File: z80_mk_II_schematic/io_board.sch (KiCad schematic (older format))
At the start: 27 parts, among them J2 Conn_02x10_Odd_Even, J3 Conn_02x08_Odd_Even, J4 Conn_02x10_Odd_Even, U12 74LS00, U13 Z80_PIO, U14 74LS245, U15 74LS145, U16 74LS245, U17 Z80_CTC, U18 74LS138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

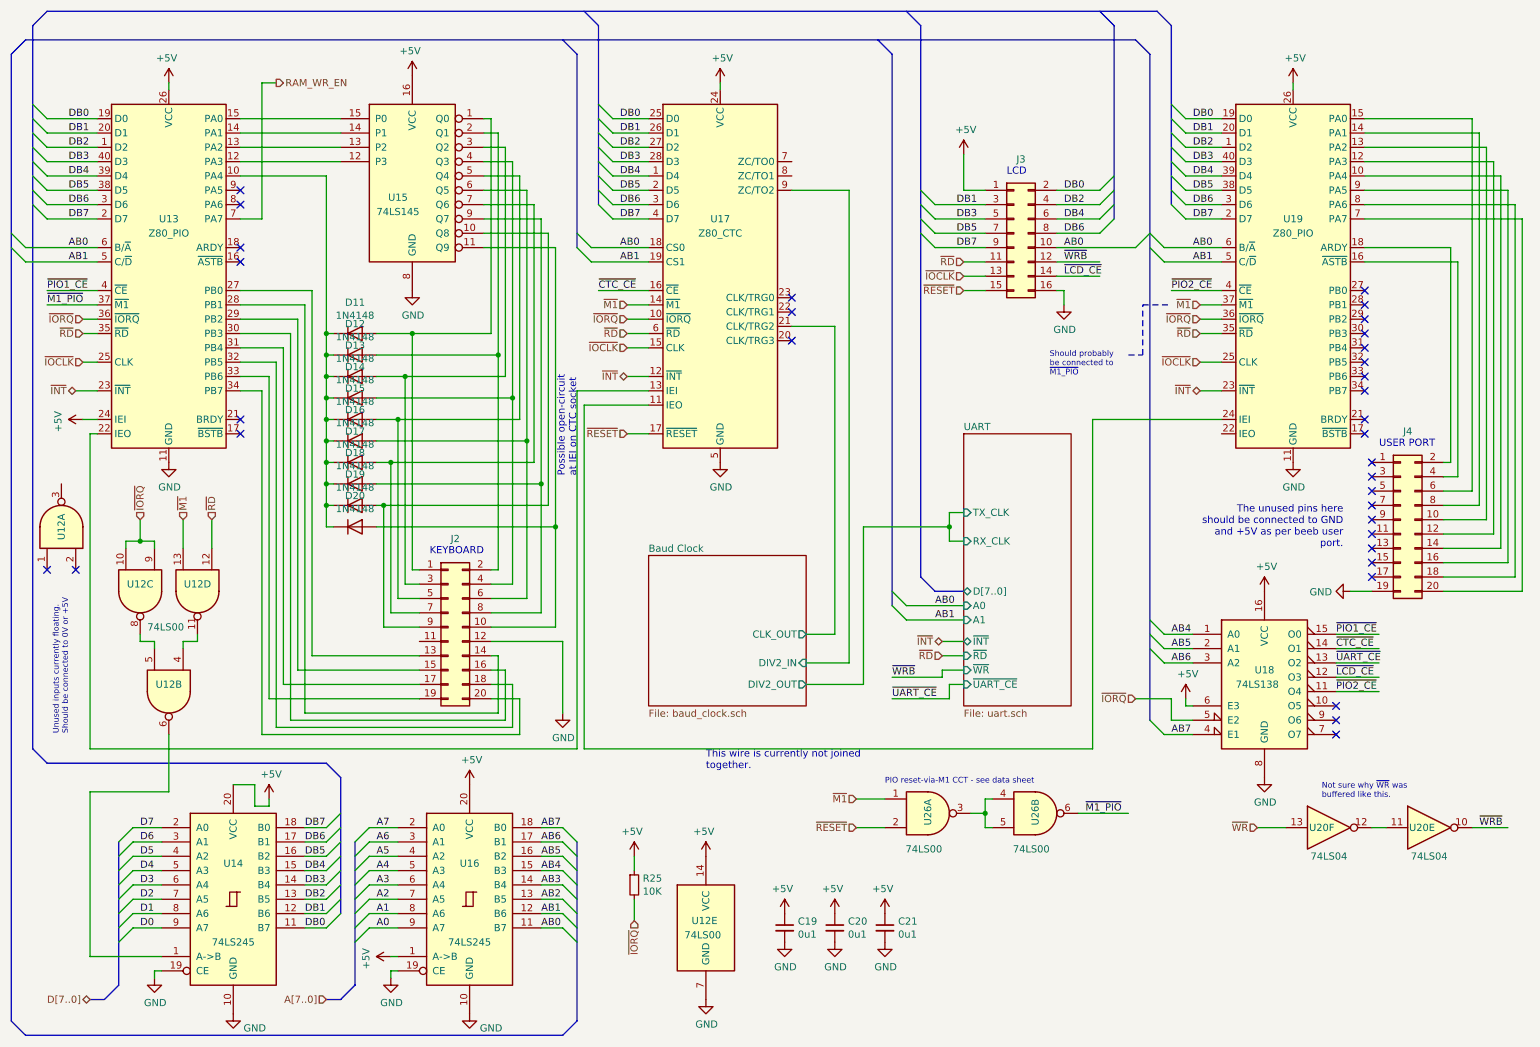
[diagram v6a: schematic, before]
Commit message: Add missing resnet for keyboard pull-ups.
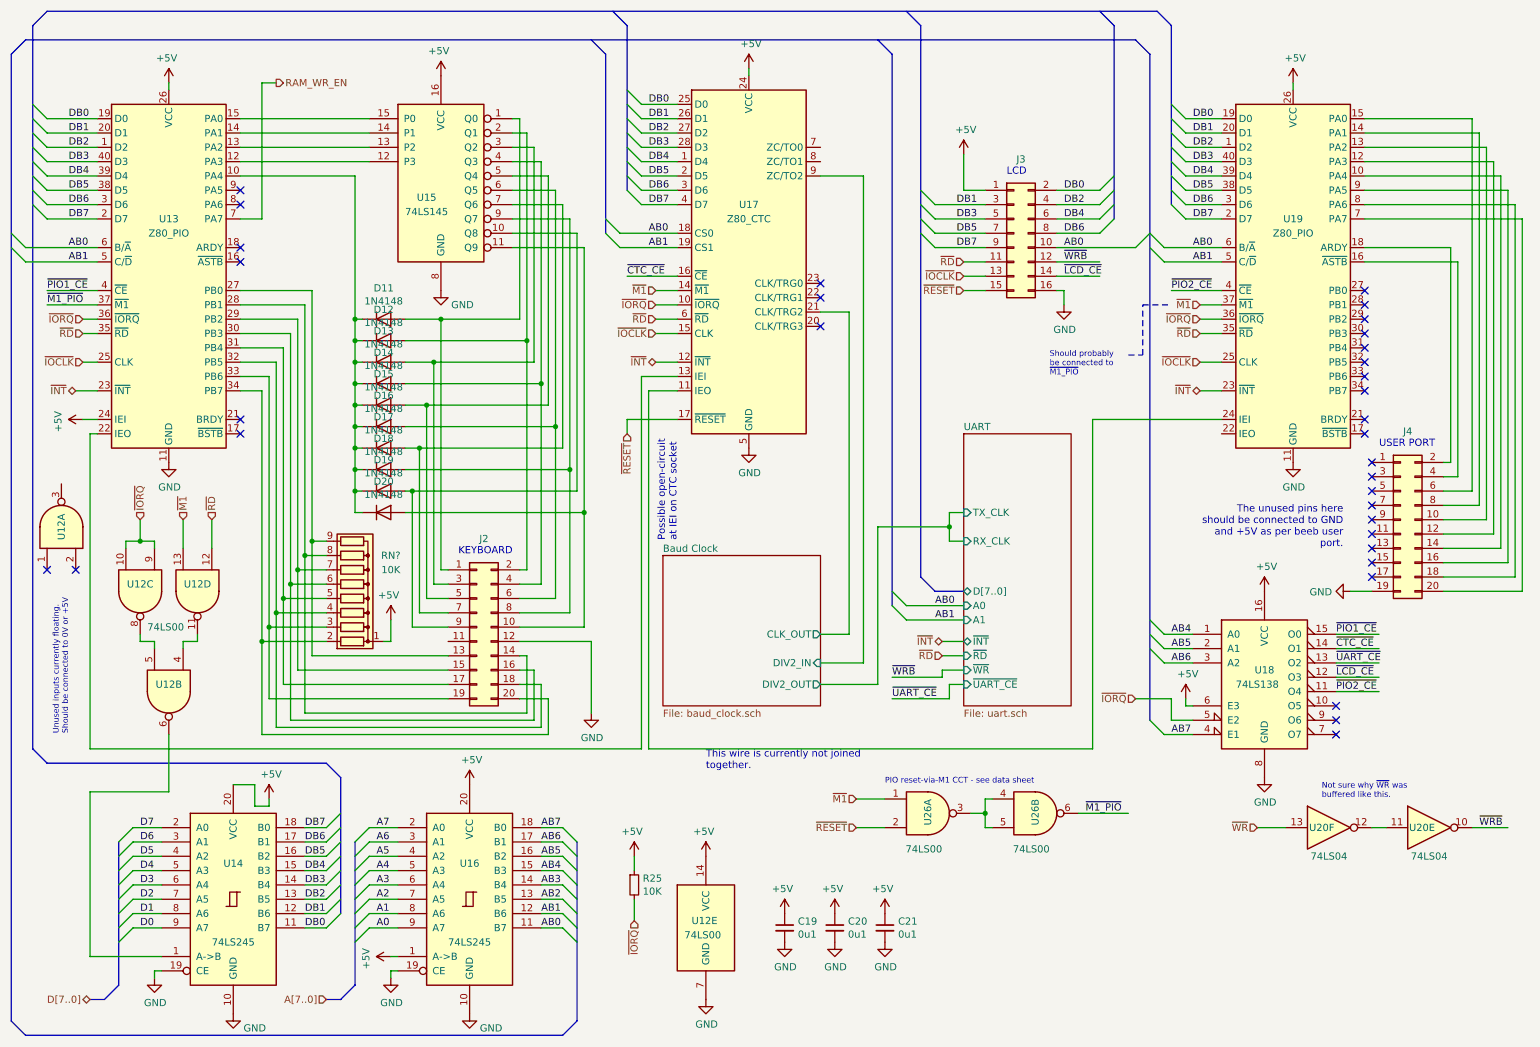
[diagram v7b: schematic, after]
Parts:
- added RN?: 10K, Resistor_THT:R_Array_SIP9, symbol Device:R_Network08
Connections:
- net +5V: now also RN?.1 (common)
- net at J2.13 (Pin_13), U13.27 (PB0): now also RN?.9 (R8)
- net at J2.14 (Pin_14), U13.28 (PB1): now also RN?.8 (R7)
- net at J2.15 (Pin_15), U13.29 (PB2): now also RN?.7 (R6)
- net at J2.16 (Pin_16), U13.30 (PB3): now also RN?.6 (R5)
- net at J2.17 (Pin_17), U13.31 (PB4): now also RN?.5 (R4)
- net at J2.18 (Pin_18), U13.32 (PB5): now also RN?.4 (R3)
- net at J2.19 (Pin_19), U13.33 (PB6): now also RN?.3 (R2)
- net at J2.20 (Pin_20), U13.34 (PB7): now also RN?.2 (R1)
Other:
- moved on the sheet: D11, D12, D13, D14, D15, D16, D17, D18, D19, D20, J2, U15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
